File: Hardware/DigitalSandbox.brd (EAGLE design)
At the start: 109.2 x 76.2 mm, 82 parts, among them J1 AVR_SPI_PRG_6NS, Q1 MOSFET-N, Q2 MOSFET-P, Q3 TRANS-11480, Q4 TRANS-11480, Q5 TRANS-11480, U1 MCP73831, U2 ATMEGA328, U3 C2031N-1A2-B10K-GP, U4 MCP9700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

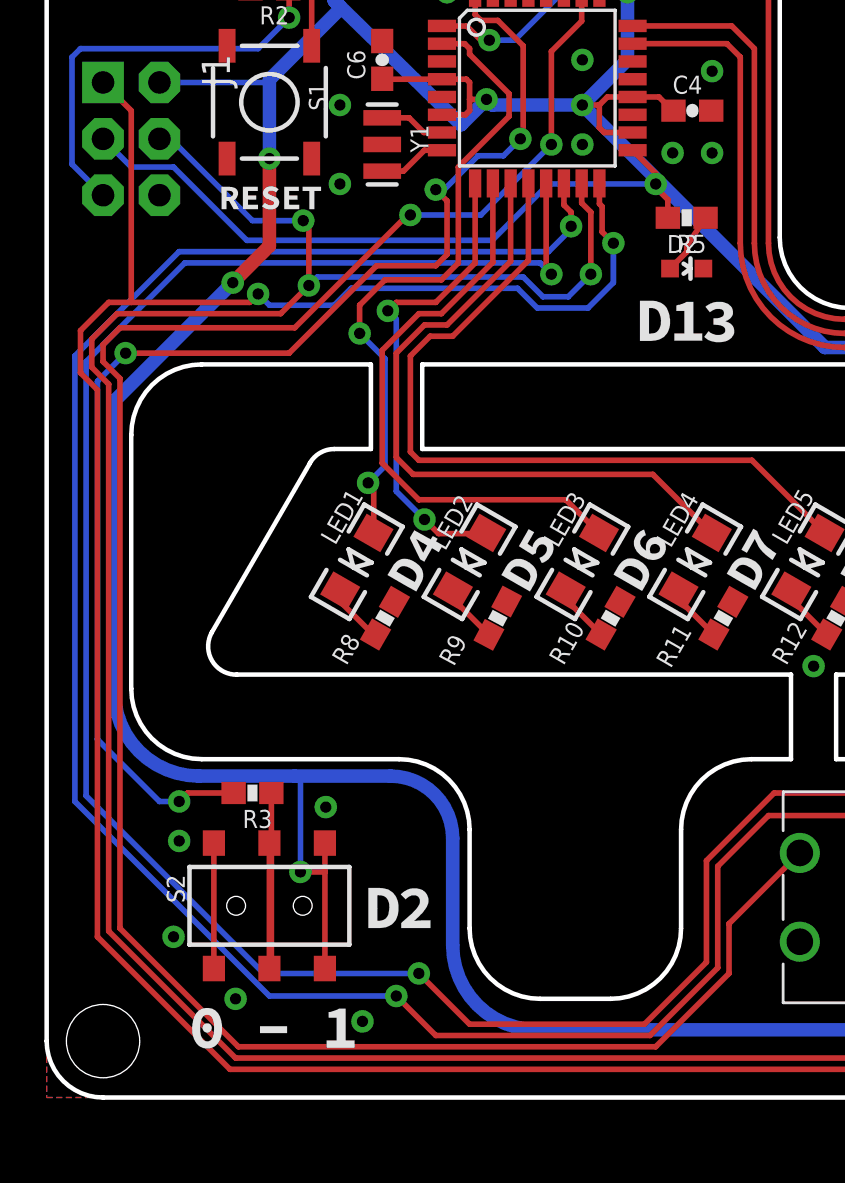
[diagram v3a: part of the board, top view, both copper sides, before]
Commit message: Corrected drill hit on power trace.
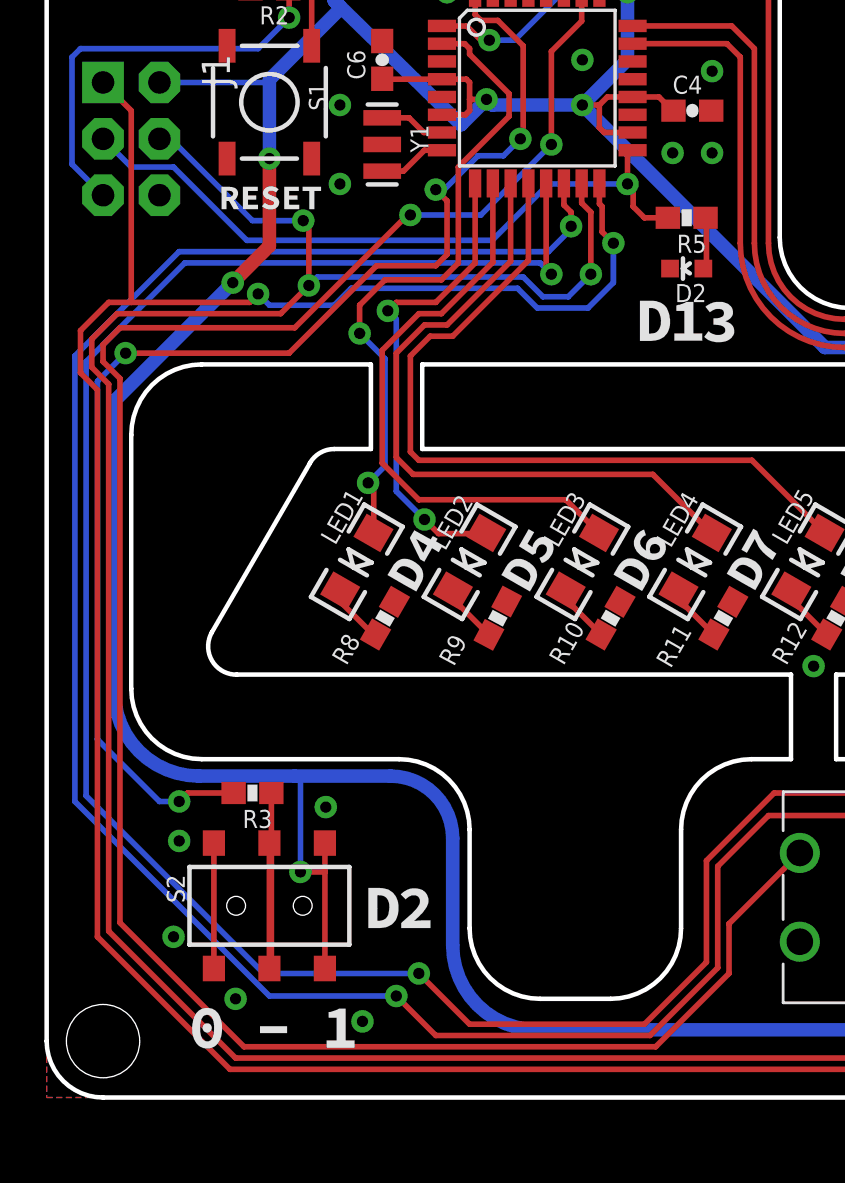
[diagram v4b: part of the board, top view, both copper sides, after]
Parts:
- turned D2 to 90 degrees
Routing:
- net GND: vias 36 -> 35
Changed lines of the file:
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@@
 <?xml version="1.0" encoding="utf-8"?>
 <!DOCTYPE eagle SYSTEM "eagle.dtd">
-<eagle version="6.5.0">
+<eagle version="6.0">
 <drawing>
 <settings>
@@
 </class>
 </classes>
-<designrules name="default">
+<designrules>
 <description language="en">&lt;b&gt;EAGLE Design Rules&lt;/b&gt;
 &lt;p&gt;
@@
 <attribute name="VALUE" x="19.558" y="39.116" size="0.8128" layer="27" font="vector" ratio="15"/>
 </element>
-<element name="D2" library="SparkFun" package="LED-0603" value="Status" x="28.829" y="37.338" smashed="yes" rot="R270">
-<attribute name="NAME" x="27.94" y="38.0365" size="0.8128" layer="25" font="vector" ratio="15"/>
-<attribute name="VALUE" x="27.813" y="36.2585" size="0.8128" layer="27" font="vector" ratio="15"/>
+<element name="D2" library="SparkFun" package="LED-0603" value="Status" x="28.829" y="37.338" smashed="yes" rot="R90">
+<attribute name="NAME" x="29.718" y="36.6395" size="0.8128" layer="25" font="vector" ratio="15" rot="R180"/>
+<attribute name="VALUE" x="30.4165" y="38.481" size="0.8128" layer="27" font="vector" ratio="15" rot="R270"/>
 </element>
 <element name="C3" library="SparkFun" package="EIA3528" value="47uF" x="28.989" y="52.4509" smashed="yes" rot="R270">
@@
 <via x="31.75" y="70.612" extent="1-16" drill="0.508"/>
 <via x="13.208" y="41.148" extent="1-16" drill="0.508"/>
-<via x="24.13" y="42.926" extent="1-16" drill="0.508"/>
 <via x="29.972" y="46.228" extent="1-16" drill="0.508"/>
 <via x="24.13" y="46.736" extent="1-16" drill="0.508"/>
@@
 <contactref element="U2" pad="17"/>
 <contactref element="R5" pad="2"/>
-<wire x1="27.979" y1="40.4426" x2="27.979" y2="39.624" width="0.254" layer="1"/>
 <wire x1="27.94" y1="39.624" x2="27.979" y2="39.624" width="0.254" layer="1"/>
 <contactref element="J1" pad="3"/>
-<via x="27.432" y="41.148" extent="1-16" drill="0.508"/>
-<wire x1="27.432" y1="41.148" x2="22.606" y2="41.148" width="0.254" layer="16"/>
+<via x="26.162" y="41.148" extent="1-16" drill="0.508"/>
+<wire x1="26.162" y1="41.148" x2="22.606" y2="41.148" width="0.254" layer="16"/>
 <wire x1="22.606" y1="41.148" x2="20.066" y2="38.608" width="0.254" layer="16"/>
 <wire x1="20.066" y1="38.608" x2="9.017" y2="38.608" width="0.254" layer="16"/>
@@
 <wire x1="5.715" y1="41.91" x2="3.81" y2="41.91" width="0.254" layer="16"/>
 <wire x1="3.81" y1="41.91" x2="2.54" y2="43.18" width="0.254" layer="16"/>
-<wire x1="27.979" y1="40.4426" x2="27.432" y2="40.9896" width="0.254" layer="1"/>
-<wire x1="27.432" y1="40.9896" x2="27.432" y2="41.148" width="0.254" layer="1"/>
-<wire x1="26.3906" y1="42.666" x2="27.432" y2="41.6246" width="0.254" layer="1"/>
-<wire x1="27.432" y1="41.6246" x2="27.432" y2="41.148" width="0.254" layer="1"/>
+<wire x1="27.979" y1="39.624" x2="26.924" y2="39.624" width="0.254" layer="1"/>
+<wire x1="26.924" y1="39.624" x2="26.416" y2="40.132" width="0.254" layer="1"/>
+<wire x1="26.416" y1="40.132" x2="26.416" y2="40.894" width="0.254" layer="1"/>
+<wire x1="26.416" y1="40.894" x2="26.162" y2="41.148" width="0.254" layer="1"/>
+<wire x1="26.3906" y1="42.666" x2="26.162" y2="42.4374" width="0.254" layer="1"/>
+<wire x1="26.162" y1="42.4374" x2="26.162" y2="41.148" width="0.254" layer="1"/>
 </signal>
 <signal name="RXD">
@@
 <contactref element="D2" pad="A"/>
 <contactref element="R5" pad="1"/>
-<wire x1="28.079" y1="37.338" x2="28.829" y2="38.088" width="0.254" layer="1"/>
-<wire x1="28.829" y1="38.088" x2="28.829" y2="38.354" width="0.254" layer="1"/>
-<wire x1="28.829" y1="38.354" x2="29.679" y2="39.624" width="0.254" layer="1"/>
+<wire x1="29.679" y1="39.624" x2="29.718" y2="39.585" width="0.254" layer="1"/>
+<wire x1="29.718" y1="39.585" x2="29.718" y2="37.338" width="0.254" layer="1"/>
+<wire x1="29.579" y1="37.338" x2="29.718" y2="37.338" width="0.254" layer="1"/>
 </signal>
 <signal name="D9">
@@
 <wire x1="16.383" y1="39.751" x2="19.558" y2="39.751" width="0.254" layer="16"/>
 <wire x1="34.449" y1="11.017" x2="33.923" y2="11.017" width="0.254" layer="16"/>
-<wire x1="8.636" y1="2.286" x2="27.432" y2="2.286" width="0.254" layer="1"/>
+<wire x1="8.89" y1="2.286" x2="27.432" y2="2.286" width="0.254" layer="1"/>
 <wire x1="27.432" y1="2.286" x2="30.734" y2="5.588" width="0.254" layer="1"/>
 <wire x1="30.734" y1="5.588" x2="30.734" y2="7.828" width="0.254" layer="1"/>
 <wire x1="30.734" y1="7.828" x2="33.923" y2="11.017" width="0.254" layer="1"/>
-<wire x1="8.636" y1="2.286" x2="3.302" y2="7.62" width="0.254" layer="1"/>
-<wire x1="3.302" y1="7.62" x2="3.302" y2="32.385" width="0.254" layer="1"/>
+<wire x1="8.89" y1="2.286" x2="3.302" y2="7.874" width="0.254" layer="1"/>
+<wire x1="3.302" y1="7.874" x2="3.302" y2="32.385" width="0.254" layer="1"/>
 </signal>
 <signal name="A4">

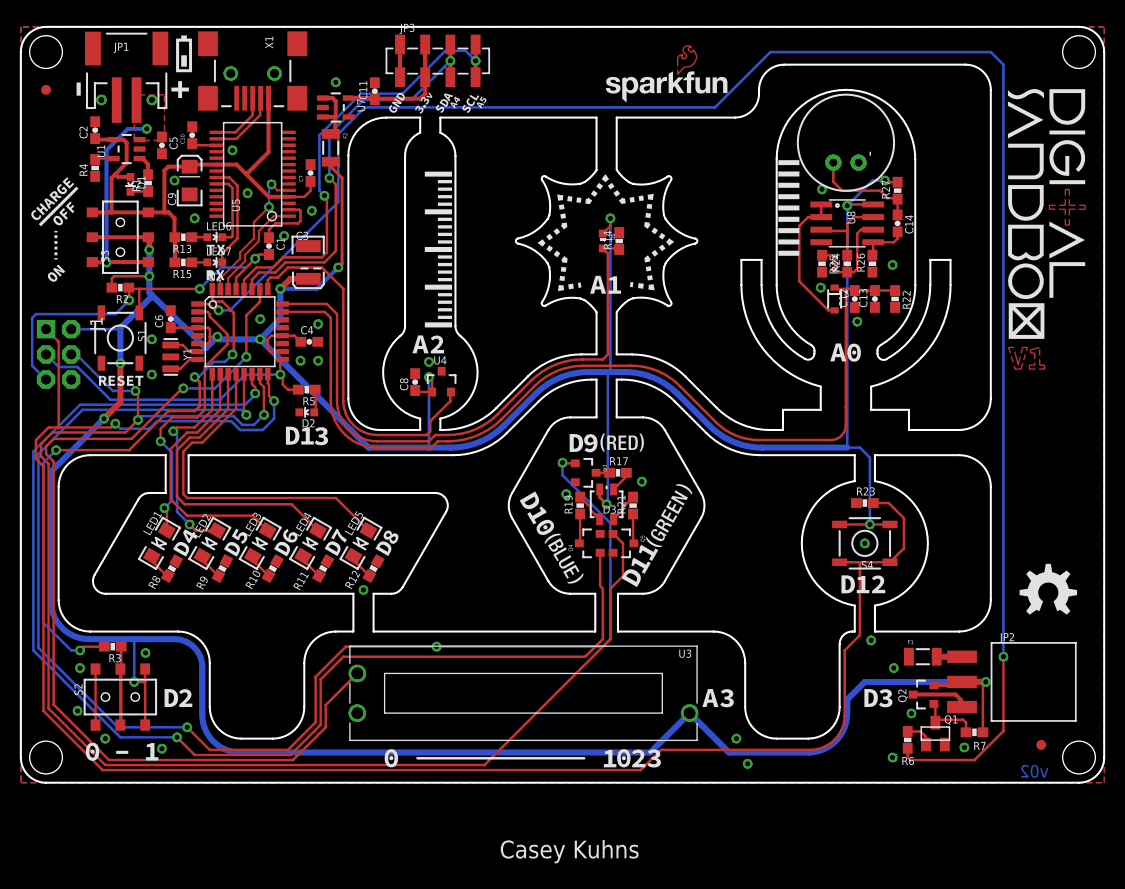
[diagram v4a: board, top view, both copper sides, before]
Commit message: Completed:
1. D13 led from 0603 yellow to 1206 Red.
2. Re-order A0 - A2.
3. Add Flyback diode on Motor port
4. Change resistor values on LED row to 330ohm to reduce intensity.
6. Label D3 output for motors and servos
7. Replace D12 pushbutton with new raised head button.
8. replace RGB LED with one spec'ed by Nate.
9. Re-order LED pins on Silk.

TODO:
5. Investigate the Microphone circuit to increase output.
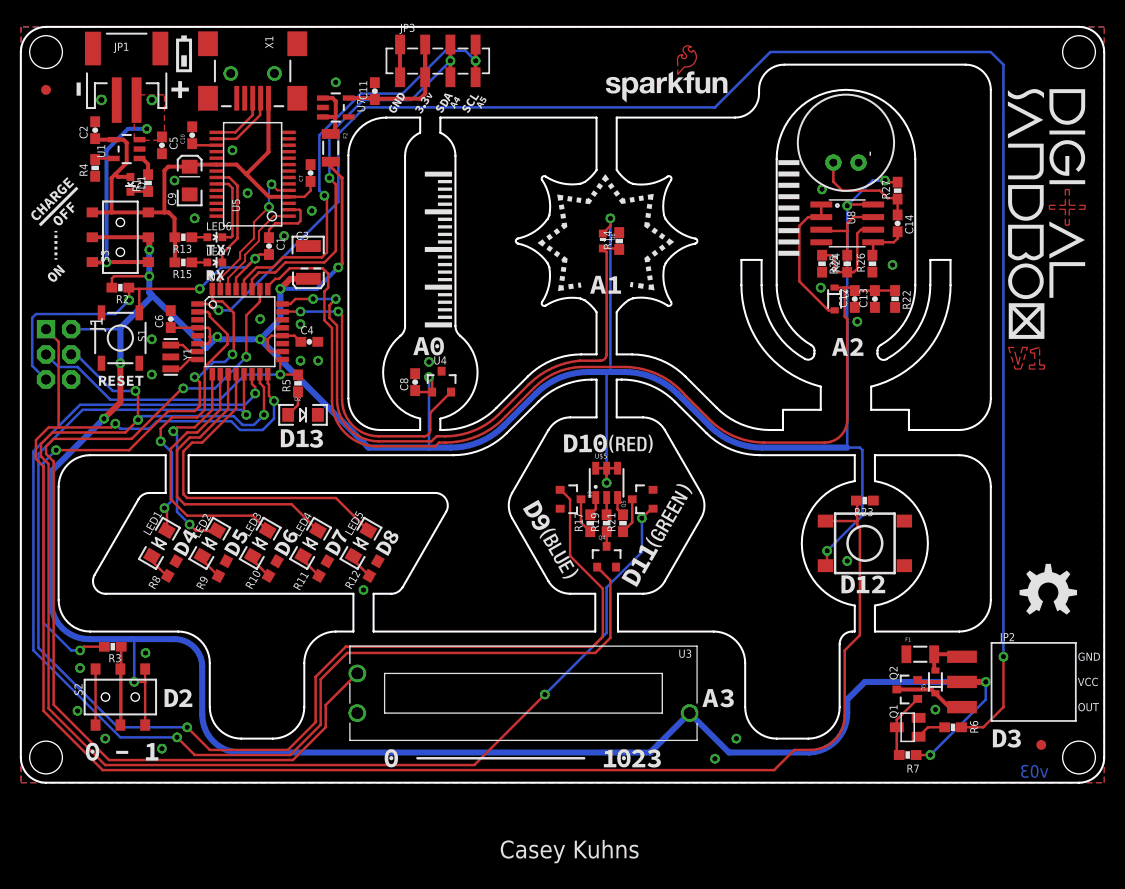
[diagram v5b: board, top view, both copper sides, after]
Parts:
- removed D3: LED-TRICOLOR, SparkFun:LED-TRICOLOR-SMD
- removed S4: (no value), SparkFun:TACTILE_SWITCH_SMD
- added D5: (no value), SparkFun-DiscreteSemi:SOD-323
- added S5: SWITCH-MOMENTARY-2SMD-4, SparkFun-Electromechanical:TACTILE_SWITCH_TALL
- added U$5: LED-TRICOLOR-SMDPLCC-6-SMD, Testing:PLCC-6-LED
- D2: value Status -> RED; device SparkFun:LED-0603 -> SparkFun-LED:LED-1206
- R10, R11, R12, R8, R9: value 100 -> 330; device SparkFun:0603-RES -> SparkFun-Resistors:0603
- moved R7 7.11 mm to (89.4, 2.79)
- moved R17 5.80 mm to (57.4, 26.2), turned to 90 degrees
- moved Q5 4.89 mm to (62.7, 28.6), turned to 90 degrees
- moved R6 4.75 mm to (94.0, 5.59), turned to 0 degrees
- moved R19 3.21 mm to (59.1, 26.2)
- moved Q3 3.07 mm to (55.4, 28.6)
- moved Q1 2.87 mm to (89.4, 5.59), turned to 90 degrees
- moved Q4 2.16 mm to (59.1, 22.7), turned to 0 degrees
- moved R21 2.05 mm to (60.7, 26.2)
- moved Q2 1.73 mm to (89.4, 9.40)
- moved R5 1.09 mm to (27.9, 40.3), turned to 90 degrees
- moved D2 0.46 mm to (28.4, 37.1), turned to 0 degrees
- moved F1 0.36 mm to (90.7, 13.0)
- moved R23 0.25 mm to (85.1, 28.4), turned to 180 degrees
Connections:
- net A0: now also U4.2; no longer C12.2, C13.2, D4.1, R22.1
- net A2: now also C12.2, C13.2, D4.C, R22.1; no longer U4.2
- net D12: now also S5.A2; no longer S4.1, S4.2
- net GRN: now also U$5.CG; no longer D3.G
- net N$16: now also D5.A
- net N$24: now also D4.A; no longer D4.2
- net N$28: now also U$5.CR; no longer D3.B
- net N$8: now also D5.C
- net RED: now also U$5.CB; no longer D3.R
- net VCC: now also S5.B2, U$5.AB, U$5.AG, U$5.AR; no longer D3.A, S4.3, S4.4
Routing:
- net A2: track 36.4 -> 99.6 mm
- net A0: track 92.7 -> 30.0 mm, vias 0 -> 2
- net D3: track 175.9 -> 166.7 mm
- net VCC: track 403.5 -> 411.6 mm, vias 16 -> 17
- net D9: track 137.1 -> 131.9 mm, vias 4 -> 2
- net D12: track 184.3 -> 180.1 mm
- net D11: track 142.5 -> 145.4 mm, vias 3 -> 5
- net N$29: track 1.35 -> 3.65 mm
- net N$16: track 2.55 -> 4.61 mm
- net N$27: track 2.99 -> 1.48 mm
- net N$8: track 5.81 -> 7.31 mm
- net A1: track 59.0 -> 60.4 mm, vias 0 -> 2
- net N$28: track 3.04 -> 1.74 mm
- net D13: track 31.1 -> 30.0 mm
- net GRN: track 3.04 -> 1.97 mm
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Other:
- board text added: "GND"
- board text added: "OUT"
- board text added: "VCC"
- board text added: "v03"
- board text removed: "v02"

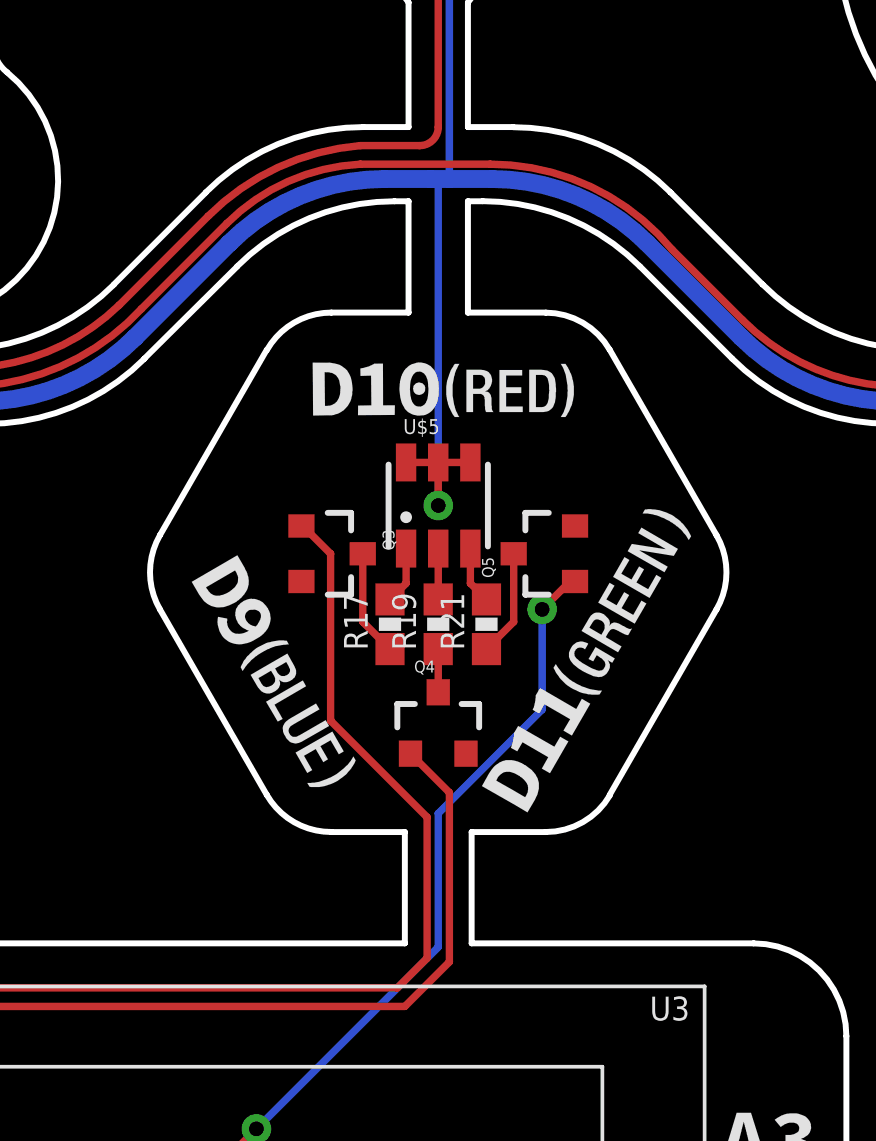
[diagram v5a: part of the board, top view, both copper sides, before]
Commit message: removed power transistors from RGB LED's.
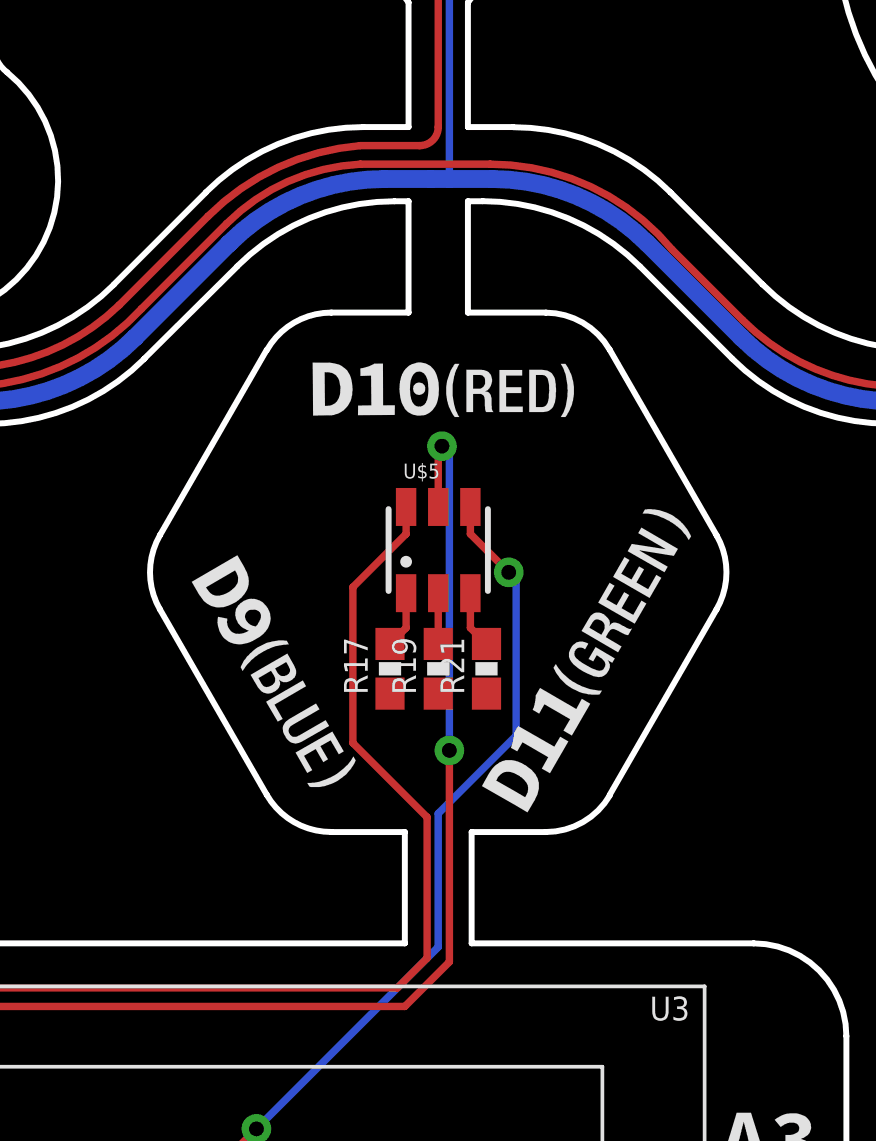
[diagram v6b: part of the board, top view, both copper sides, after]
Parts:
- removed Q3, Q4, Q5: TRANS-11480, SparkFun-DiscreteSemi:SOT23-3
- moved R17 1.52 mm to (57.4, 24.6)
- moved R19 1.52 mm to (59.1, 24.6)
- moved R21 1.52 mm to (60.7, 24.6)
- moved U$5 1.52 mm to (59.1, 28.7)
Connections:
- removed net N$25: Q5.3, R21.1
- removed net N$27: Q4.3, R19.1
- removed net N$29: Q3.3, R17.1
- net D10: now also U$5.AR; no longer Q4.1
- net D11: now also U$5.AG; no longer Q5.1
- net D9: now also U$5.AB; no longer Q3.1
- net GND: now also R17.1, R19.1, R21.1; no longer Q3.2, Q4.2, Q5.2
- net VCC: no longer U$5.AB, U$5.AG, U$5.AR
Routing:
- net VCC: track 411.6 -> 396.8 mm, vias 17 -> 16
- net D10: track 124.9 -> 137.1 mm, vias 2 -> 4
- net N$29: track 3.65 -> 0.00 mm
- net N$25: track 3.65 -> 0.00 mm
- net D11: track 145.4 -> 148.2 mm
- net N$27: track 1.48 -> 0.00 mm
- net D9: track 131.9 -> 132.6 mm
